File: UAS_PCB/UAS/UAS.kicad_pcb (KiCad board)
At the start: 2 copper layers, 50.8 x 47.6 mm, 17 parts, among them J1 SM02B-PASS-TBT, J2 SM02B-PASS-TBT, J3 SM02B-PASS-TBT, J4 SM02B-PASS-TBT, U1 JST-7-Pin, U10 UAS-rescue_7.5V-2.4A-Converte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, U2 5A-5V-Converter, U3 500mA-5V-Converter, U4 12V-StepUp-Converter, U5 TB6612FNG-Dual-Motor-Driver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

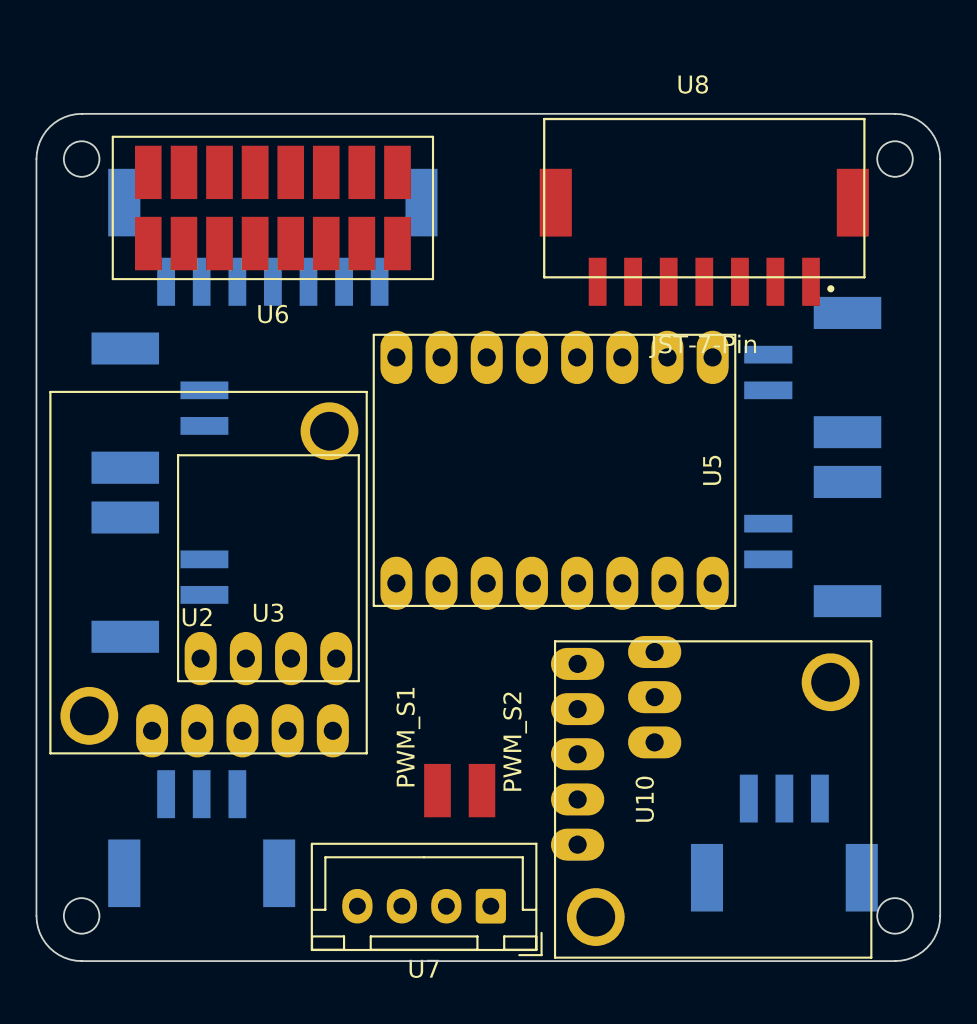
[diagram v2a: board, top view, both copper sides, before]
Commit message: fixed courtyard errors
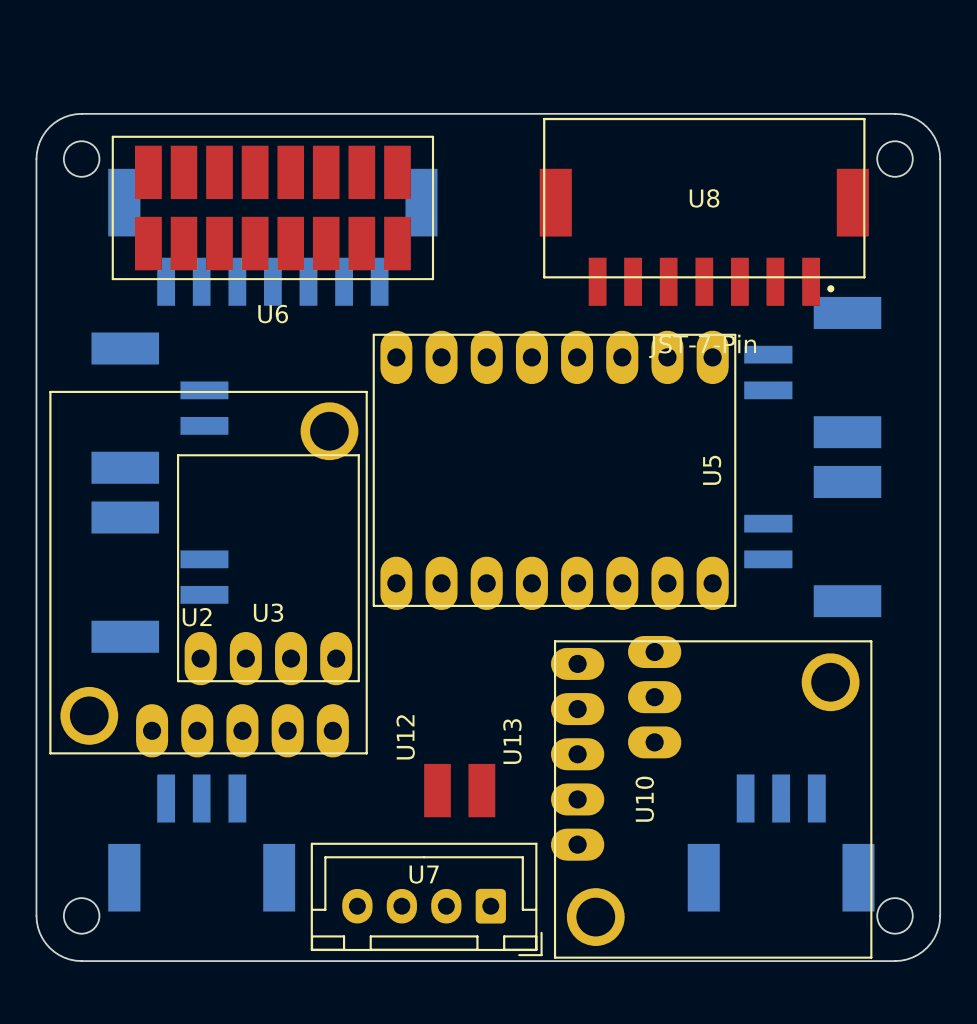
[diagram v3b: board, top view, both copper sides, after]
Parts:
- removed Servo 2: JST-3-Pin, UAS:JST_SM03B-PASS-TBT(LF)(SN)
- added U9: JST-3-Pin, UAS:JST_SM03B-PASS-TBT(LF)(SN), B.Cu at (159.3, 121.0)
- U11: renamed from Servo 1
- moved U11 0.25 mm to (126.8, 121.0)
- renumbered PWM_S1 to U12, PWM_S2 to U13
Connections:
- U7 pad 1: Net-(U10-Pad4) -> Net-(U10-Pad3)
- U7 pad 4: Net-(U10-Pad3) -> Net-(U10-Pad4)
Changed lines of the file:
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@@
   (module UAS:Individual_Solder_Pad (layer Front)
     (at 142.5 111.5)
-    (fp_text reference PWM_S2 (at 1.75 -2.75 90 unlocked) (layer F.SilkS)
+    (fp_text reference U13 (at 1.75 -2.75 90) (layer F.SilkS)
       (effects (font (size 1 1) (thickness 0.15)))
     )
@@
       (effects (font (size 1 1) (thickness 0.15)))
     )
+    (fp_line (start -0.75 1.5) (end -0.75 -1.5) (layer F.CrtYd) (width 0.12))
+    (fp_line (start -0.75 -1.5) (end 0.75 -1.5) (layer F.CrtYd) (width 0.12))
+    (fp_line (start 0.75 -1.5) (end 0.75 1.5) (layer F.CrtYd) (width 0.12))
+    (fp_line (start 0.75 1.5) (end -0.75 1.5) (layer F.CrtYd) (width 0.12))
     (pad 1 smd rect (at 0 0) (size 1.5 3) (layers Front F.Paste F.Mask)
       (net 33 "Net-(U13-Pad1)"))
@@
   (module UAS:Individual_Solder_Pad (layer Front)
     (at 140 111.5)
-    (fp_text reference PWM_S1 (at -1.75 -3 90 unlocked) (layer F.SilkS)
+    (fp_text reference U12 (at -1.75 -3 90) (layer F.SilkS)
       (effects (font (size 1 1) (thickness 0.15)))
     )
@@
       (effects (font (size 1 1) (thickness 0.15)))
     )
+    (fp_line (start -0.75 1.5) (end -0.75 -1.5) (layer F.CrtYd) (width 0.12))
+    (fp_line (start -0.75 -1.5) (end 0.75 -1.5) (layer F.CrtYd) (width 0.12))
+    (fp_line (start 0.75 -1.5) (end 0.75 1.5) (layer F.CrtYd) (width 0.12))
+    (fp_line (start 0.75 1.5) (end -0.75 1.5) (layer F.CrtYd) (width 0.12))
     (pad 1 smd rect (at 0 0) (size 1.5 3) (layers Front F.Paste F.Mask)
       (net 32 "Net-(U11-Pad3)"))
+  )
+  (module UAS:16_Pad_Set_2mm_pitch (layer Front)
+    (at 130.75 76.75 180)
+    (fp_text reference U6 (at 0 -8) (layer F.SilkS)
+      (effects (font (size 1 1) (thickness 0.15)))
+    )
+    (fp_text value 16_Pad_2x8_Set (at 0 5) (layer F.Fab)
+      (effects (font (size 1 1) (thickness 0.15)))
+    )
+    (fp_line (start -9 2) (end -9 -6) (layer F.SilkS) (width 0.12))
+    (fp_line (start 9 -6) (end 9 2) (layer F.SilkS) (width 0.12))
+    (fp_line (start -9 2) (end 9 2) (layer F.SilkS) (width 0.12))
+    (fp_line (start 9 -6) (end -9 -6) (layer F.SilkS) (width 0.12))
+    (fp_poly (pts (xy 0.25 -5.75) (xy -0.25 -5.75) (xy -0.25 -6) (xy 0.25 -6)) (layer F.CrtYd) (width 0.1))
+    (pad 16 smd rect (at 7 0 180) (size 1.5 3) (layers Front F.Paste F.Mask)
+      (net 12 "Net-(U1-Pad7)"))
+    (pad 15 smd rect (at 7 -4 180) (size 1.5 3) (layers Front F.Paste F.Mask)
+      (net 12 "Net-(U1-Pad7)"))
+    (pad 14 smd rect (at 5 0 180) (size 1.5 3) (layers Front F.Paste F.Mask)
+      (net 11 "Net-(U1-Pad6)"))
+    (pad 13 smd rect (at 5 -4 180) (size 1.5 3) (layers Front F.Paste F.Mask)
+      (net 11 "Net-(U1-Pad6)"))
+    (pad 12 smd rect (at 3 0 180) (size 1.5 3) (layers Front F.Paste F.Mask)
+      (net 5 "Net-(J3-Pad1)"))
+    (pad 11 smd rect (at 3 -4 180) (size 1.5 3) (layers Front F.Paste F.Mask)
+      (net 5 "Net-(J3-Pad1)"))
+    (pad 10 smd rect (at 1 0 180) (size 1.5 3) (layers Front F.Paste F.Mask)
+      (net 6 "Net-(J3-Pad2)"))
+    (pad 9 smd rect (at 1 -4 180) (size 1.5 3) (layers Front F.Paste F.Mask)
+      (net 6 "Net-(J3-Pad2)"))
+    (pad 8 smd rect (at -1 0 180) (size 1.5 3) (layers Front F.Paste F.Mask)
+      (net 8 "Net-(U1-Pad5)"))
+    (pad 7 smd rect (at -1 -4 180) (size 1.5 3) (layers Front F.Paste F.Mask)
+      (net 8 "Net-(U1-Pad5)"))
+    (pad 6 smd rect (at -3 0 180) (size 1.5 3) (layers Front F.Paste F.Mask)
+      (net 7 "Net-(U1-Pad4)"))
+    (pad 5 smd rect (at -3 -4 180) (size 1.5 3) (layers Front F.Paste F.Mask)
+      (net 7 "Net-(U1-Pad4)"))
+    (pad 4 smd rect (at -5 0 180) (size 1.5 3) (layers Front F.Paste F.Mask)
+      (net 9 "Net-(U1-Pad3)"))
+    (pad 3 smd rect (at -5 -4 180) (size 1.5 3) (layers Front F.Paste F.Mask)
+      (net 9 "Net-(U1-Pad3)"))
+    (pad 2 smd rect (at -7 0 180) (size 1.5 3) (layers Front F.Paste F.Mask)
+      (net 10 "Net-(U1-Pad2)"))
+    (pad 1 smd rect (at -7 -4 180) (size 1.5 3) (layers Front F.Paste F.Mask)
+      (net 13 "Net-(U1-Pad1)"))
   )
   (module UAS:Pololu_7.75V_2.4A_Step_Down_Regulator (layer Front)
@@
   )
   (module "UAS:JST_SM03B-PASS-TBT(LF)(SN)" (layer Back)
-    (at 126.75 120.75)
-    (fp_text reference "Servo 1" (at 0 -3.75) (layer B.SilkS)
+    (at 126.75 121)
+    (fp_text reference U11 (at 0 -3.75) (layer B.SilkS)
       (effects (font (size 1 1) (thickness 0.015)) (justify mirror))
     )
@@
   )
   (module "UAS:JST_SM03B-PASS-TBT(LF)(SN)" (layer Back)
-    (at 159.5 121)
-    (fp_text reference "Servo 2" (at 0 -3.75) (layer B.SilkS)
+    (at 159.3215 121)
+    (fp_text reference U9 (at 0 -3.75) (layer B.SilkS)
       (effects (font (size 1 1) (thickness 0.015)) (justify mirror))
     )
@@
   (module "UAS:JST_SM07B-PASS-TBT(LF)(SN)" (layer Front)
     (at 155 73.75)
-    (fp_text reference U8 (at -0.635 -1.905) (layer F.SilkS)
+    (fp_text reference U8 (at 0 4.5) (layer F.SilkS)
       (effects (font (size 1 1) (thickness 0.015)))
     )
@@
     (descr "JST XH series connector, B4B-XH-A (http://www.jst-mfg.com/product/pdf/eng/eXH.pdf), generated with kicad-footprint-generator")
     (tags "connector JST XH vertical")
-    (fp_text reference U7 (at 3.75 -3.55) (layer F.SilkS)
+    (fp_text reference U7 (at 3.75 1.75) (layer F.SilkS)
       (effects (font (size 1 1) (thickness 0.15)))
     )
@@
     )
     (pad 4 thru_hole oval (at 7.5 0 180) (size 1.7 1.95) (drill 0.95) (layers *.Cu *.Mask)
-      (net 15 "Net-(U10-Pad3)"))
+      (net 14 "Net-(U10-Pad4)"))
     (pad 3 thru_hole oval (at 5 0 180) (size 1.7 1.95) (drill 0.95) (layers *.Cu *.Mask)
       (net 27 "Net-(U7-Pad3)"))
@@
       (net 28 "Net-(U7-Pad2)"))
     (pad 1 thru_hole roundrect (at 0 0 180) (size 1.7 1.95) (drill 0.95) (layers *.Cu *.Mask) (roundrect_rratio 0.147059)
-      (net 14 "Net-(U10-Pad4)"))
+      (net 15 "Net-(U10-Pad3)"))
     (model ${KISYS3DMOD}/Connector_JST.3dshapes/JST_XH_B4B-XH-A_1x04_P2.50mm_Vertical.wrl
       (at (xyz 0 0 0))
@@
       (rotate (xyz 0 0 0))
     )
-  )
-  (module UAS:16_Pad_Set_2mm_pitch (layer Front)
-    (at 130.75 76.75 180)
-    (fp_text reference U6 (at 0 -8) (layer F.SilkS)
-      (effects (font (size 1 1) (thickness 0.15)))
-    )
-    (fp_text value 16_Pad_2x8_Set (at 0 5) (layer F.Fab)
-      (effects (font (size 1 1) (thickness 0.15)))
-    )
-    (fp_line (start 9 -6) (end -9 -6) (layer F.SilkS) (width 0.12))
-    (fp_line (start -9 2) (end 9 2) (layer F.SilkS) (width 0.12))
-    (fp_line (start 9 -6) (end 9 2) (layer F.SilkS) (width 0.12))
-    (fp_line (start -9 2) (end -9 -6) (layer F.SilkS) (width 0.12))
-    (pad 16 smd rect (at 7 0 180) (size 1.5 3) (layers Front F.Paste F.Mask)
-      (net 12 "Net-(U1-Pad7)"))
-    (pad 15 smd rect (at 7 -4 180) (size 1.5 3) (layers Front F.Paste F.Mask)
-      (net 12 "Net-(U1-Pad7)"))
-    (pad 14 smd rect (at 5 0 180) (size 1.5 3) (layers Front F.Paste F.Mask)
-      (net 11 "Net-(U1-Pad6)"))
-    (pad 13 smd rect (at 5 -4 180) (size 1.5 3) (layers Front F.Paste F.Mask)
-      (net 11 "Net-(U1-Pad6)"))
-    (pad 12 smd rect (at 3 0 180) (size 1.5 3) (layers Front F.Paste F.Mask)
-      (net 5 "Net-(J3-Pad1)"))
-    (pad 11 smd rect (at 3 -4 180) (size 1.5 3) (layers Front F.Paste F.Mask)
-      (net 5 "Net-(J3-Pad1)"))
-    (pad 10 smd rect (at 1 0 180) (size 1.5 3) (layers Front F.Paste F.Mask)
-      (net 6 "Net-(J3-Pad2)"))
-    (pad 9 smd rect (at 1 -4 180) (size 1.5 3) (layers Front F.Paste F.Mask)
-      (net 6 "Net-(J3-Pad2)"))
-    (pad 8 smd rect (at -1 0 180) (size 1.5 3) (layers Front F.Paste F.Mask)
-      (net 8 "Net-(U1-Pad5)"))
-    (pad 7 smd rect (at -1 -4 180) (size 1.5 3) (layers Front F.Paste F.Mask)
-      (net 8 "Net-(U1-Pad5)"))
-    (pad 6 smd rect (at -3 0 180) (size 1.5 3) (layers Front F.Paste F.Mask)
-      (net 7 "Net-(U1-Pad4)"))
-    (pad 5 smd rect (at -3 -4 180) (size 1.5 3) (layers Front F.Paste F.Mask)
-      (net 7 "Net-(U1-Pad4)"))
-    (pad 4 smd rect (at -5 0 180) (size 1.5 3) (layers Front F.Paste F.Mask)
-      (net 9 "Net-(U1-Pad3)"))
-    (pad 3 smd rect (at -5 -4 180) (size 1.5 3) (layers Front F.Paste F.Mask)
-      (net 9 "Net-(U1-Pad3)"))
-    (pad 2 smd rect (at -7 0 180) (size 1.5 3) (layers Front F.Paste F.Mask)
-      (net 10 "Net-(U1-Pad2)"))
-    (pad 1 smd rect (at -7 -4 180) (size 1.5 3) (layers Front F.Paste F.Mask)
-      (net 13 "Net-(U1-Pad1)"))
   )
   (module UAS:Pololu_TB6612_Dual_Motor_Driver_Carrier (layer Front)
@@
   (module "UAS:JST_SM07B-PASS-TBT(LF)(SN)" (layer Back)
     (at 130.75 73.75 180)
-    (fp_text reference U1 (at -0.635 1.905) (layer B.SilkS)
+    (fp_text reference U1 (at 0.25 -5) (layer B.SilkS)
       (effects (font (size 1 1) (thickness 0.015)) (justify mirror))
     )
@@
   (module "UAS:JST_SM02B-PASS-TBT(LF)(SN)" (layer Back)
     (at 123 90 270)
-    (fp_text reference J4 (at -0.825 6.735 270) (layer B.SilkS)
+    (fp_text reference J4 (at 0.25 1 270) (layer B.SilkS)
       (effects (font (size 1 1) (thickness 0.015)) (justify mirror))
     )
@@
   (module "UAS:JST_SM02B-PASS-TBT(LF)(SN)" (layer Back)
     (at 123 99.5 270)
-    (fp_text reference J3 (at -0.825 6.735 270) (layer B.SilkS)
+    (fp_text reference J3 (at 0 1 270) (layer B.SilkS)
       (effects (font (size 1 1) (thickness 0.015)) (justify mirror))
     )
@@
   (module "UAS:JST_SM02B-PASS-TBT(LF)(SN)" (layer Back)
     (at 162.5 97.5 90)
-    (fp_text reference J2 (at -0.825 6.735 270) (layer B.SilkS)
+    (fp_text reference J2 (at 0 0.5 270) (layer B.SilkS)
       (effects (font (size 1 1) (thickness 0.015)) (justify mirror))
     )
@@
   (module "UAS:JST_SM02B-PASS-TBT(LF)(SN)" (layer Back)
     (at 162.5 88 90)
-    (fp_text reference J1 (at -0.825 6.735 270) (layer B.SilkS)
-      (effects (font (size 1 1) (thickness 0.015)) (justify mirror))
-    )
+    (fp_text reference J1 (at 0 0.5 270) (layer B.SilkS)
+      (effects (font (size 1 1) (thickness 0.015)) (justify mirror))
+    )

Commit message: SMT TB6612
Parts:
- U5: footprint UAS:Pololu_TB6612_Dual_Motor_Driver_Carrier -> UAS:Pololu_TB6612_Dual_Motor_Driver_Carrier_SMT
- moved U5 9.50 mm to (151.0, 93.5)

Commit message: First traces
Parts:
- U5: footprint UAS:Pololu_TB6612_Dual_Motor_Driver_Carrier_SMT -> UAS:Pololu_TB6612_Dual_Motor_Driver_Carrier
- moved U13 17.8 mm to (159.5, 116.8)
- moved U12 14.2 mm to (126.7, 116.5)
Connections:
- net Net-(U10-Pad4) renamed GND
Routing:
- net Net-(U10-Pad3): track 0.00 -> 49.9 mm
- net Net-(U10-Pad5): track 0.00 -> 38.6 mm
- net Net-(J3-Pad2): track 0.00 -> 31.1 mm, vias 0 -> 2
- net Net-(J3-Pad1): track 0.00 -> 22.5 mm, vias 0 -> 2
- net Net-(U4-Pad3): track 0.00 -> 12.4 mm
- net Net-(U13-Pad1): track 0.00 -> 7.55 mm, vias 0 -> 1
- net Net-(U11-Pad3): track 0.00 -> 5.93 mm, vias 0 -> 1
- net GND: track 0.00 -> 5.71 mm, vias 0 -> 4

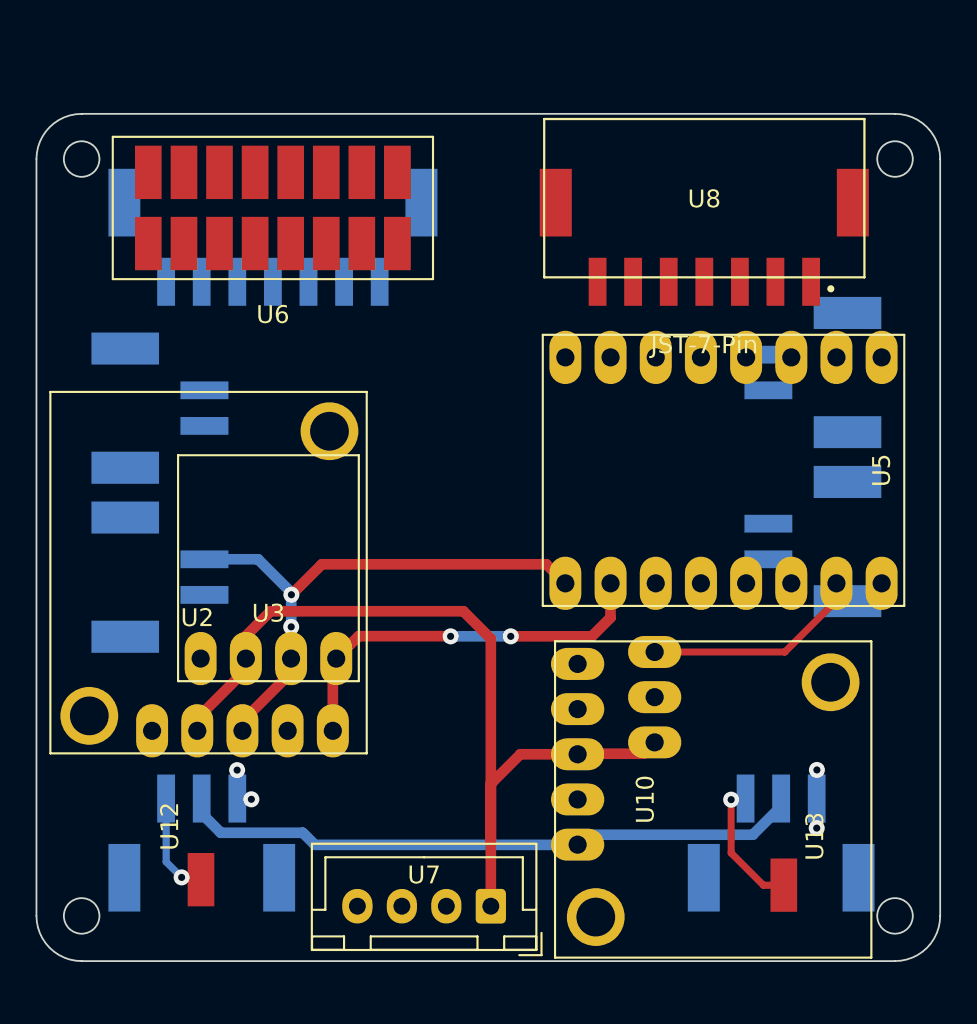
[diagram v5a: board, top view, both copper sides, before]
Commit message: Routing Traces
All traces besides the top connectors are routed, but the top connector pads need to be rearranged. The ground plane still need to be placed. Trace widths still need to be set.
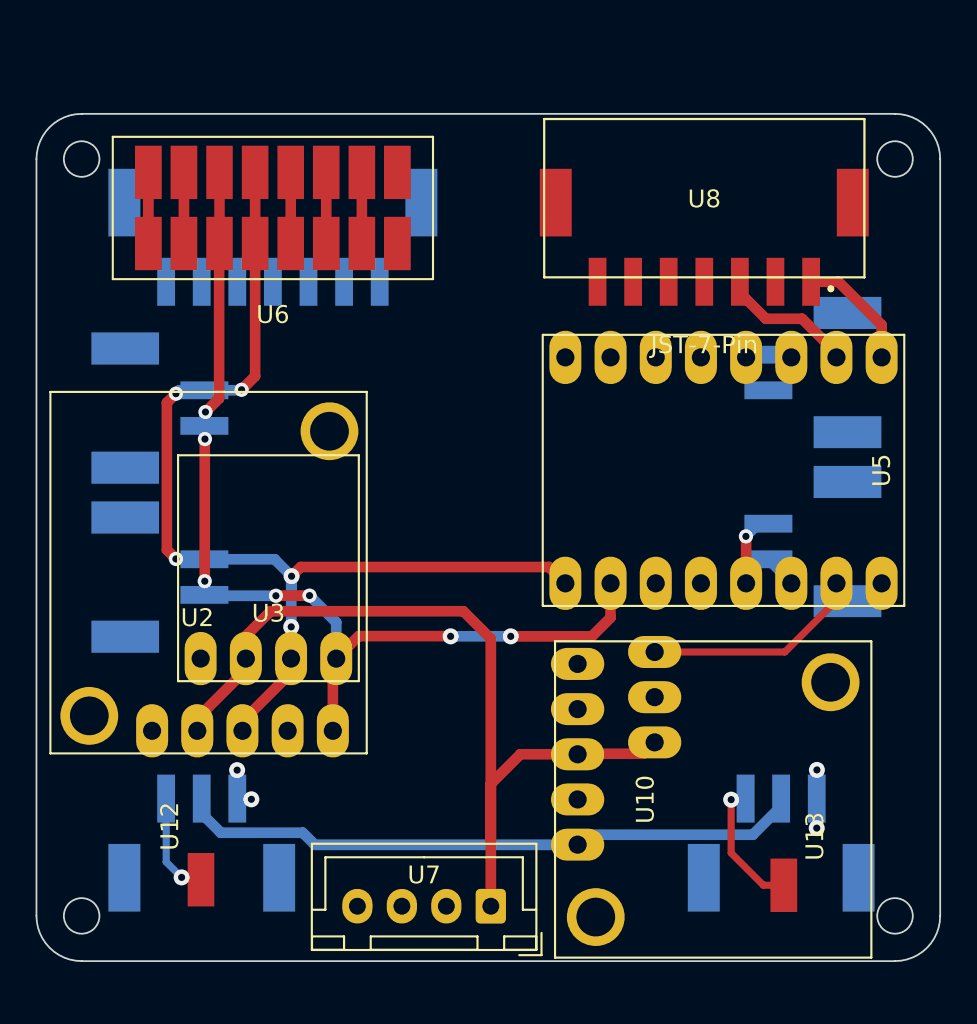
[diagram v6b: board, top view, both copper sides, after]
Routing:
- net Net-(J3-Pad1): track 22.5 -> 56.7 mm, vias 2 -> 7
- net Net-(J3-Pad2): track 31.1 -> 59.7 mm, vias 2 -> 5
- net Net-(U5-Pad15): track 0.00 -> 7.69 mm
- net Net-(U5-Pad16): track 0.00 -> 6.80 mm
- net Net-(J2-Pad1): track 0.00 -> 4.26 mm, vias 0 -> 1
- net Net-(U1-Pad7): track 0.00 -> 4.00 mm
- net Net-(U1-Pad6): track 0.00 -> 4.00 mm
- net Net-(U1-Pad5): track 0.00 -> 4.00 mm
- net Net-(U1-Pad4): track 0.00 -> 4.00 mm
- net Net-(U1-Pad3): track 0.00 -> 4.00 mm
- net Net-(J2-Pad2): track 0.00 -> 1.88 mm
